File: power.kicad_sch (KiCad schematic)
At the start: 16 parts, among them Q1 AONM7421, SW1 SW_SPDT, U1 AZ1117-5.0, U2 AZ1117-3.3

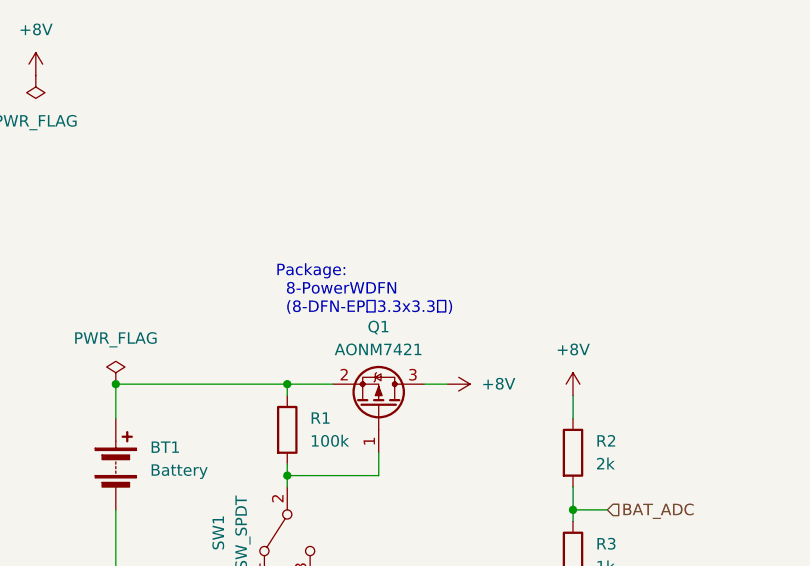
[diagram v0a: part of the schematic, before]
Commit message: AON7421のシンボル差し替え
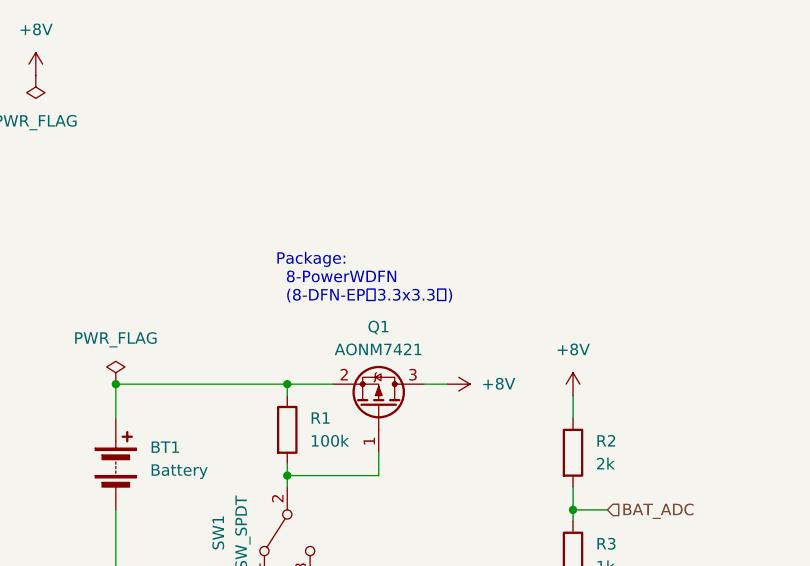
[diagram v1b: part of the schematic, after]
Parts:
- Q1: footprint (none) -> AON7421:AON7421
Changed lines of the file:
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@@
     (effects (font (size 1.27 1.27)) (justify left bottom))
   )
-  (text "Package:\n  8-PowerWDFN \n  (8-DFN-EP（3.3x3.3）)" (at 88.9 81.28 0)
+  (text "Package:\n  8-PowerWDFN \n  (8-DFN-EP（3.3x3.3）)" (at 88.9 80.01 0)
     (effects (font (size 1.27 1.27)) (justify left bottom))
   )
@@
       (effects (font (size 1.27 1.27)))
     )
-    (property "Footprint" "" (at 98.425 86.36 0)
+    (property "Footprint" "AON7421:AON7421" (at 98.425 86.36 0)
       (effects (font (size 1.27 1.27) italic) (justify left) hide)
     )
